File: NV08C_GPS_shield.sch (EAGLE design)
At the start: 43 parts, among them IC1 74LVC1T45SOT23-HAND, IC2 74LVC1T45SOT23-HAND, IC3 74LVC1T45SOT23-HAND, IC4 74LVC1T45SOT23-HAND, IC5 74LVC1T45SOT23-HAND, IC6 74LVC1T45SOT23-HAND, IC7 MCP1702-3.3, X1 CONN-SMATHD-SMD-EDGE

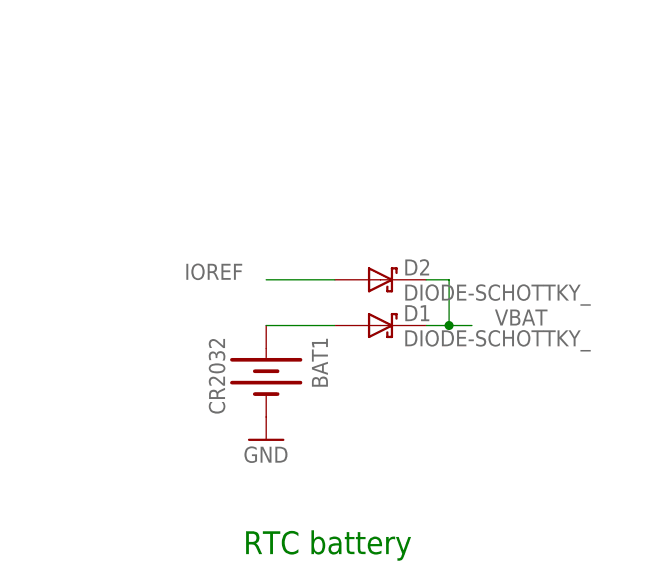
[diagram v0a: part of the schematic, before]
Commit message: Changed BAS32L to BAV70.
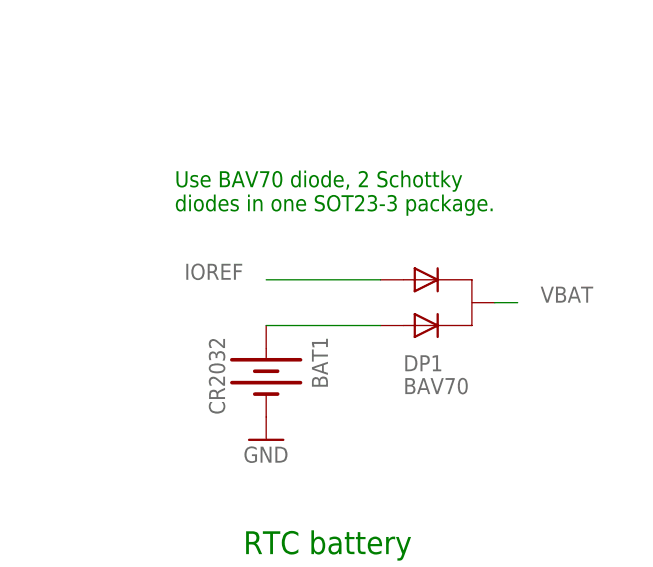
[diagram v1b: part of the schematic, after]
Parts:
- removed D1, D2: DIODE-SCHOTTKY_, SteveMarple:DIODE-SCHOTTKY_
- added DP1: BAV70, SteveMarple:DIODE-PAIR-COMMON-CATHODE
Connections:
- net IOREF: now also DP1.A1; no longer D2.A
- net VBAT: now also DP1.C; no longer D1.C, D2.C
- net VBATT: now also DP1.A2; no longer D1.A
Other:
- note added: "Use BAV70 diode, 2 Schottky diodes in one SOT23-3 package."
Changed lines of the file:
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@@
 <?xml version="1.0" encoding="utf-8"?>
 <!DOCTYPE eagle SYSTEM "eagle.dtd">
-<eagle version="6.5.0">
+<eagle version="6.4">
 <drawing>
 <settings>
@@
 <layers>
 <layer number="1" name="Top" color="4" fill="1" visible="no" active="no"/>
+<layer number="2" name="Route2" color="1" fill="3" visible="no" active="no"/>
+<layer number="3" name="Route3" color="4" fill="3" visible="no" active="no"/>
+<layer number="14" name="Route14" color="1" fill="6" visible="no" active="no"/>
+<layer number="15" name="Route15" color="4" fill="6" visible="no" active="no"/>
 <layer number="16" name="Bottom" color="1" fill="1" visible="no" active="no"/>
 <layer number="17" name="Pads" color="2" fill="1" visible="no" active="no"/>
@@
 <part name="R3" library="SteveMarple" deviceset="RESISTOR" device="1206-HAND" value="100k"/>
 <part name="R2" library="SteveMarple" deviceset="RESISTOR" device="1206-HAND" value="100k"/>
-<part name="D1" library="SteveMarple" deviceset="DIODE-SCHOTTKY" device="_"/>
-<part name="D2" library="SteveMarple" deviceset="DIODE-SCHOTTKY" device="_"/>
 <part name="JP6" library="SparkFun" deviceset="JUMPER-3" device="PTH" value="ISP VCC"/>
 <part name="P+5" library="supply1" deviceset="+5V" device=""/>
@@
 <part name="C5" library="SteveMarple" deviceset="C-EU" device="1206-HAND" value="1u"/>
 <part name="C6" library="SteveMarple" deviceset="C-EU" device="1206-HAND" value="1u"/>
+<part name="DP1" library="SteveMarple" deviceset="DIODE-PAIR-COMMON-CATHODE" device="" value="BAV70"/>
 </parts>
 <sheets>
@@
 <text x="38.1" y="30.48" size="1.778" layer="94">Add other INT pin for Mega</text>
 <text x="38.1" y="106.68" size="1.778" layer="94">Decide upon !RESET! pin</text>
+<text x="327.66" y="165.1" size="1.778" layer="91">Use BAV70 diode, 2 Schottky
+diodes in one SOT23-3 package.</text>
 </plain>
 <instances>
@@
 <instance part="R3" gate="G$1" x="91.44" y="96.52" rot="R90"/>
 <instance part="R2" gate="G$1" x="91.44" y="66.04" rot="R90"/>
-<instance part="D1" gate="G$1" x="350.52" y="152.4"/>
-<instance part="D2" gate="G$1" x="350.52" y="157.48"/>
 <instance part="JP6" gate="G$1" x="269.24" y="170.18" rot="MR0"/>
 <instance part="P+5" gate="1" x="284.48" y="165.1" rot="R270"/>
@@
 <instance part="C5" gate="G$1" x="124.46" y="215.9"/>
 <instance part="C6" gate="G$1" x="157.48" y="215.9"/>
+<instance part="DP1" gate="D$1" x="358.14" y="154.94"/>
 </instances>
 <busses>
@@
 </segment>
 <segment>
-<pinref part="D2" gate="G$1" pin="A"/>
-<wire x1="345.44" y1="157.48" x2="337.82" y2="157.48" width="0.1524" layer="91"/>
 <label x="335.28" y="157.48" size="1.778" layer="95" rot="MR0"/>
+<pinref part="DP1" gate="D$1" pin="A1"/>
+<wire x1="350.52" y1="157.48" x2="337.82" y2="157.48" width="0.1524" layer="91"/>
 </segment>
 <segment>
@@
 </segment>
 <segment>
-<pinref part="D1" gate="G$1" pin="C"/>
-<wire x1="355.6" y1="152.4" x2="358.14" y2="152.4" width="0.1524" layer="91"/>
-<label x="363.22" y="152.4" size="1.778" layer="95"/>
-<junction x="358.14" y="152.4"/>
-<wire x1="358.14" y1="152.4" x2="360.68" y2="152.4" width="0.1524" layer="91"/>
-<wire x1="358.14" y1="152.4" x2="358.14" y2="157.48" width="0.1524" layer="91"/>
-<pinref part="D2" gate="G$1" pin="C"/>
-<wire x1="358.14" y1="157.48" x2="355.6" y2="157.48" width="0.1524" layer="91"/>
+<label x="368.3" y="154.94" size="1.778" layer="95"/>
+<pinref part="DP1" gate="D$1" pin="C"/>
+<wire x1="363.22" y1="154.94" x2="365.76" y2="154.94" width="0.1524" layer="91"/>
 </segment>
 </net>
@@
 <net name="VBATT" class="0">
 <segment>
-<wire x1="337.82" y1="152.4" x2="345.44" y2="152.4" width="0.1524" layer="91"/>
+<wire x1="337.82" y1="152.4" x2="350.52" y2="152.4" width="0.1524" layer="91"/>
 <pinref part="BAT1" gate="G$1" pin="+"/>
-<pinref part="D1" gate="G$1" pin="A"/>
+<pinref part="DP1" gate="D$1" pin="A2"/>
 </segment>
 </net>
@@
 </schematic>
 </drawing>
+<compatibility>
+<note version="6.3" minversion="6.2.2" severity="warning">
+Since Version 6.2.2 text objects can contain more than one line,
+which will not be processed correctly with this version.
+</note>
+</compatibility>
 </eagle>

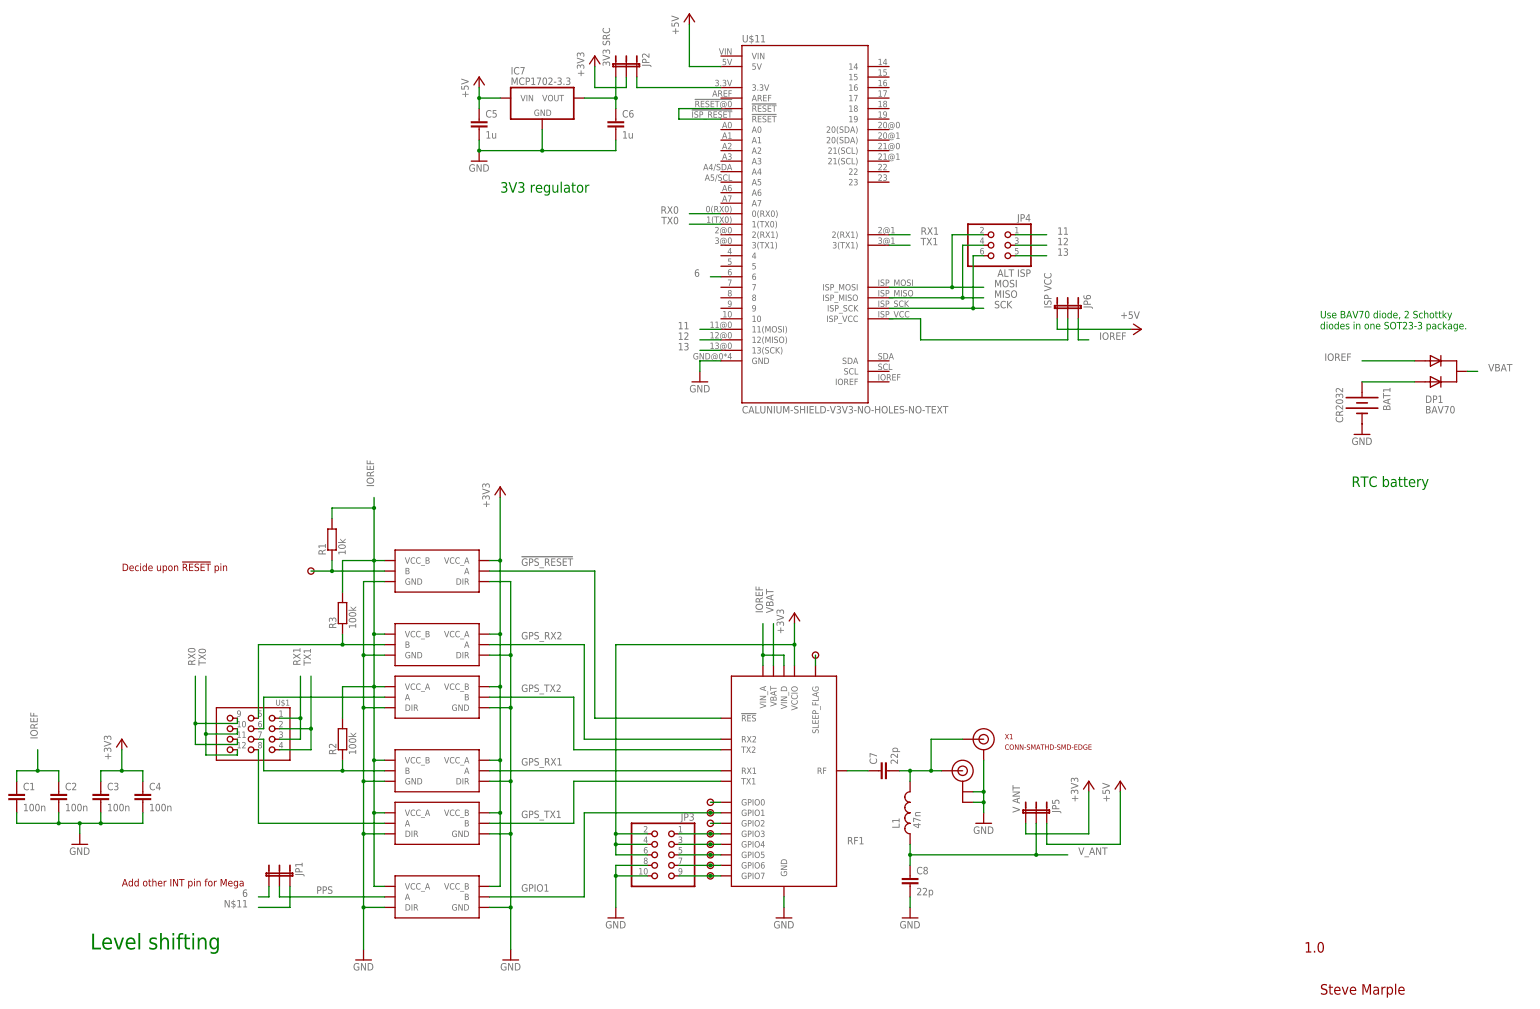
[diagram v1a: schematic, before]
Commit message: Switching to 0805 packages for some parts.
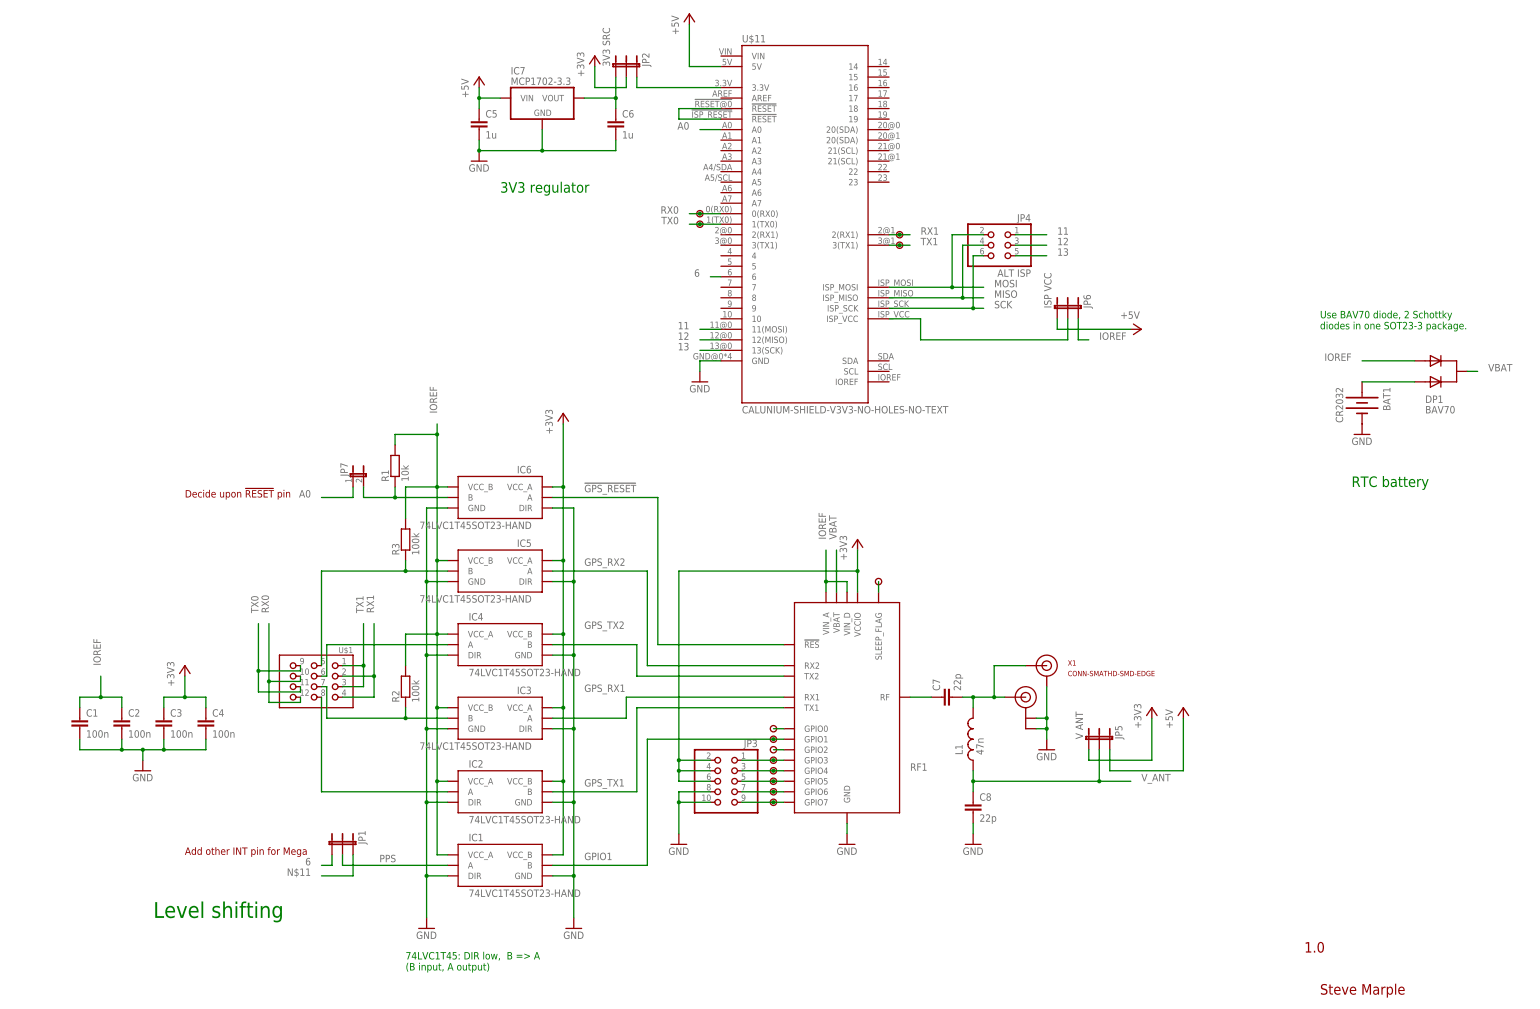
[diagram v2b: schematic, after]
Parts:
- removed U$2: PAD, SteveMarple:PAD
- added JP7: (no value), SparkFun:JUMPER-2PTH
- added U$14, U$15, U$16, U$17: PAD, SteveMarple:PAD
- C7, C8: device SteveMarple:C-EU1206-HAND -> SteveMarple:C-EU0805-HAND
- L1: device SteveMarple:INDUCTOR0805 -> SteveMarple:INDUCTOR0805-HAND
- R1: device SteveMarple:RESISTOR1206-HAND -> SteveMarple:RESISTOR0805-HAND
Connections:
- new net A0: JP7.1, U$11.A0
- net N$8: now also JP7.2; no longer U$2.1
- net RX0: now also U$1.10, U$1.12, U$14.1; no longer U$1.11, U$1.9
- net RX1: now also U$1.2, U$1.4, U$16.1; no longer U$1.1, U$1.3
- net TX0: now also U$1.11, U$1.9, U$15.1; no longer U$1.10, U$1.12
- net TX1: now also U$1.1, U$1.3, U$17.1; no longer U$1.2, U$1.4
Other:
- note added: "74LVC1T45: DIR low, B => A (B input, A output)"
- moved on the sheet: C1, C2, C3, C4, C7, C8, JP1, JP3, JP5, L1, R1, R2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

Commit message: Layout changes and some missing pin connections made.
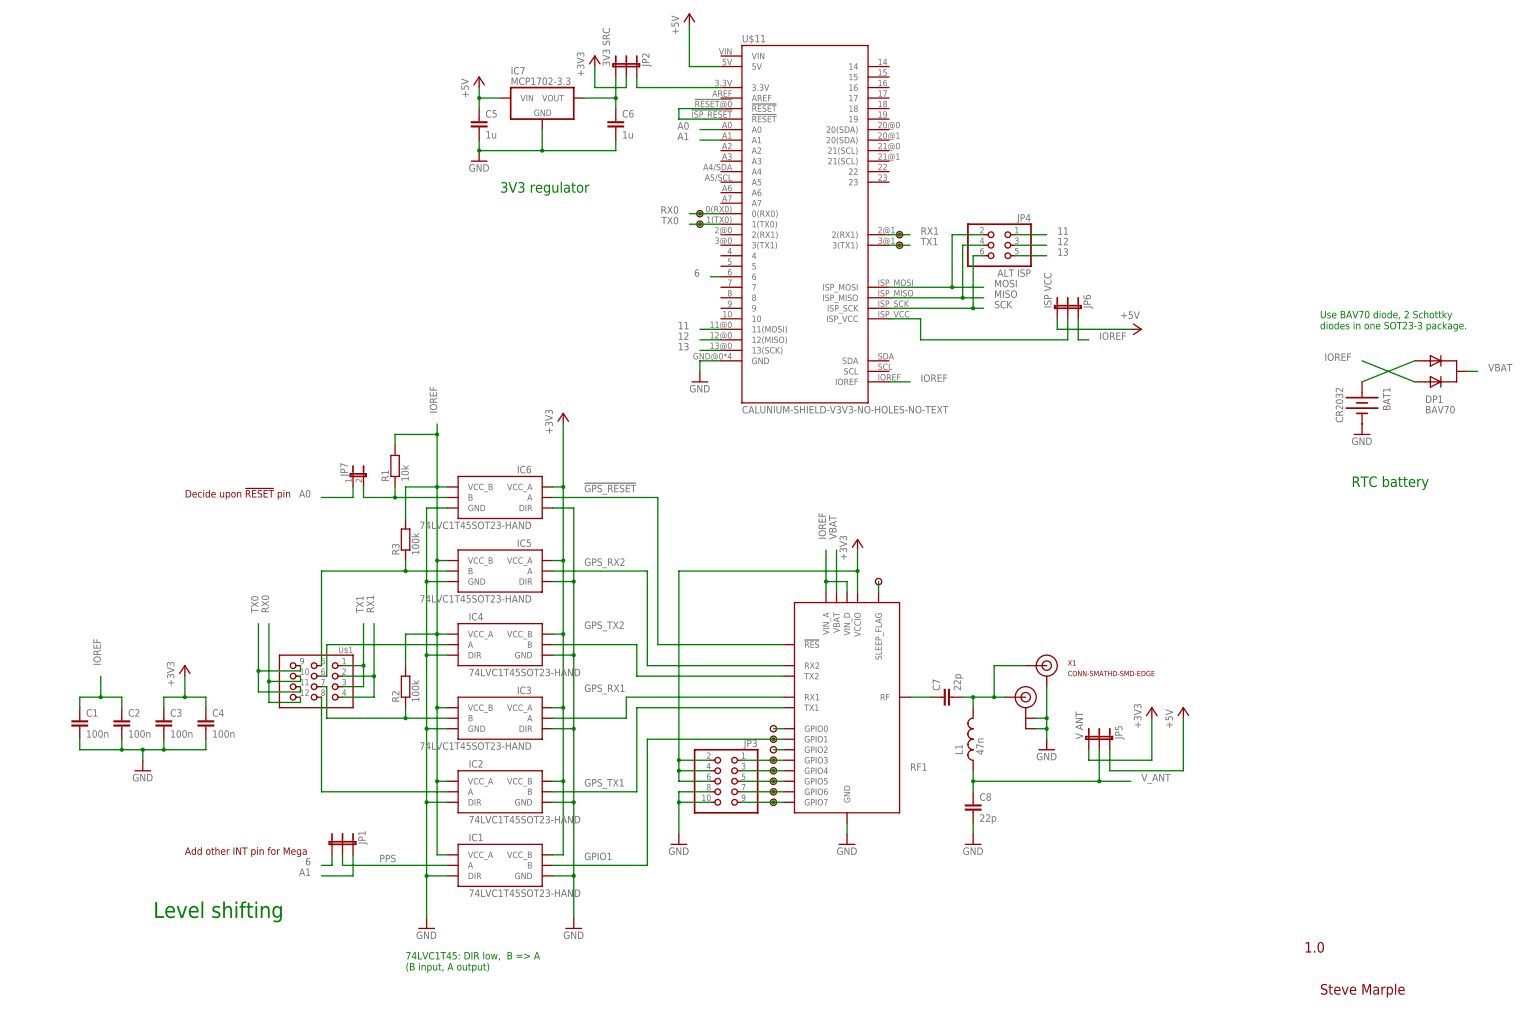
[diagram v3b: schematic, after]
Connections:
- removed net N$11: JP1.1
- new net A1: JP1.1, U$11.A1
- net IOREF: now also DP1.A2, U$11.IOREF; no longer DP1.A1
- net VBATT: now also DP1.A1; no longer DP1.A2
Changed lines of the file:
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@@
 <segment>
 <label x="335.28" y="157.48" size="1.778" layer="95" rot="MR0"/>
-<pinref part="DP1" gate="D$1" pin="A1"/>
-<wire x1="350.52" y1="157.48" x2="337.82" y2="157.48" width="0.1524" layer="91"/>
+<pinref part="DP1" gate="D$1" pin="A2"/>
+<wire x1="350.52" y1="152.4" x2="337.82" y2="157.48" width="0.1524" layer="91"/>
 </segment>
 <segment>
@@
 <wire x1="33.02" y1="76.2" x2="33.02" y2="81.28" width="0.1524" layer="91"/>
 <label x="33.02" y="83.82" size="1.778" layer="95" rot="R90"/>
+</segment>
+<segment>
+<pinref part="U$11" gate="G$1" pin="IOREF"/>
+<wire x1="223.52" y1="152.4" x2="228.6" y2="152.4" width="0.1524" layer="91"/>
+<label x="231.14" y="152.4" size="1.778" layer="95"/>
 </segment>
 </net>
@@
 <net name="VBATT" class="0">
 <segment>
-<wire x1="337.82" y1="152.4" x2="350.52" y2="152.4" width="0.1524" layer="91"/>
+<wire x1="337.82" y1="152.4" x2="350.52" y2="157.48" width="0.1524" layer="91"/>
 <pinref part="BAT1" gate="G$1" pin="+"/>
-<pinref part="DP1" gate="D$1" pin="A2"/>
+<pinref part="DP1" gate="D$1" pin="A1"/>
 </segment>
 </net>
@@
 </segment>
 </net>
-<net name="N$11" class="0">
+<net name="A1" class="0">
 <segment>
 <pinref part="JP1" gate="G$1" pin="1"/>
@@
 <label x="83.82" y="33.02" size="1.778" layer="95" rot="MR0"/>
 </segment>
-</net>
+<segment>
+<pinref part="U$11" gate="G$1" pin="A1"/>
+<wire x1="182.88" y1="210.82" x2="177.8" y2="210.82" width="0.1524" layer="91"/>
+<label x="175.26" y="210.82" size="1.778" layer="95" rot="MR0"/>
+</segment>
+</net>
